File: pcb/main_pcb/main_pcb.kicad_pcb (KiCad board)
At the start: 2 copper layers, 80 x 100 mm, 58 parts, among them J1 Conn_01x05, J10 Conn_01x06_Male, J11 Conn_01x04, J12 Screw_Terminal_01x02, J13 Conn_01x02_Male, J2 Conn_01x05, J3 Conn_01x05, J4 Conn_01x05, J5 Conn_01x05, J6 Conn_01x05, J7 Conn_01x04, J8 Conn_01x06_Male, J9 Conn_01x04, Q1 Q_PMOS_GDS, SW1 SW_SPDT, U1 LSM6DSO, U2 Teensy_4.1, U3 DRV8833, U4 LM1117-3.3, U5 TPIC74101

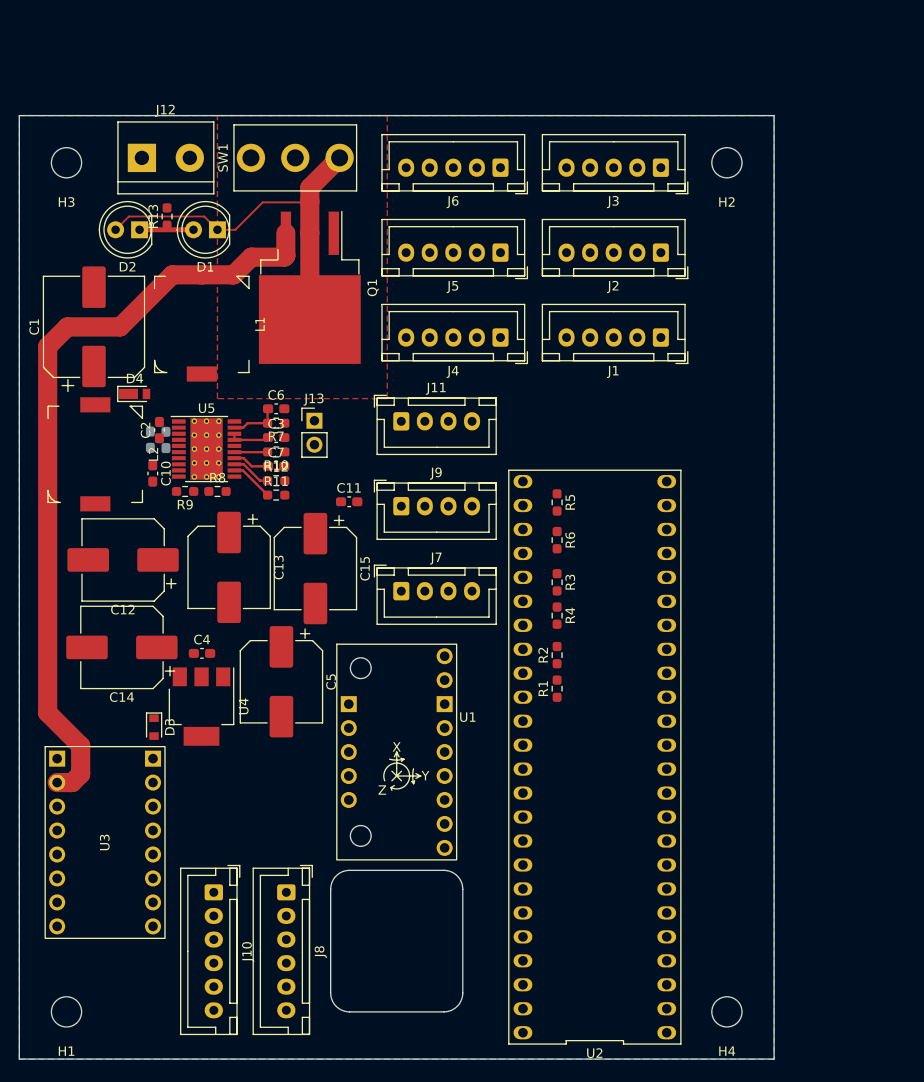
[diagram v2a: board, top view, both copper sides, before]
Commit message: Complete digital routing
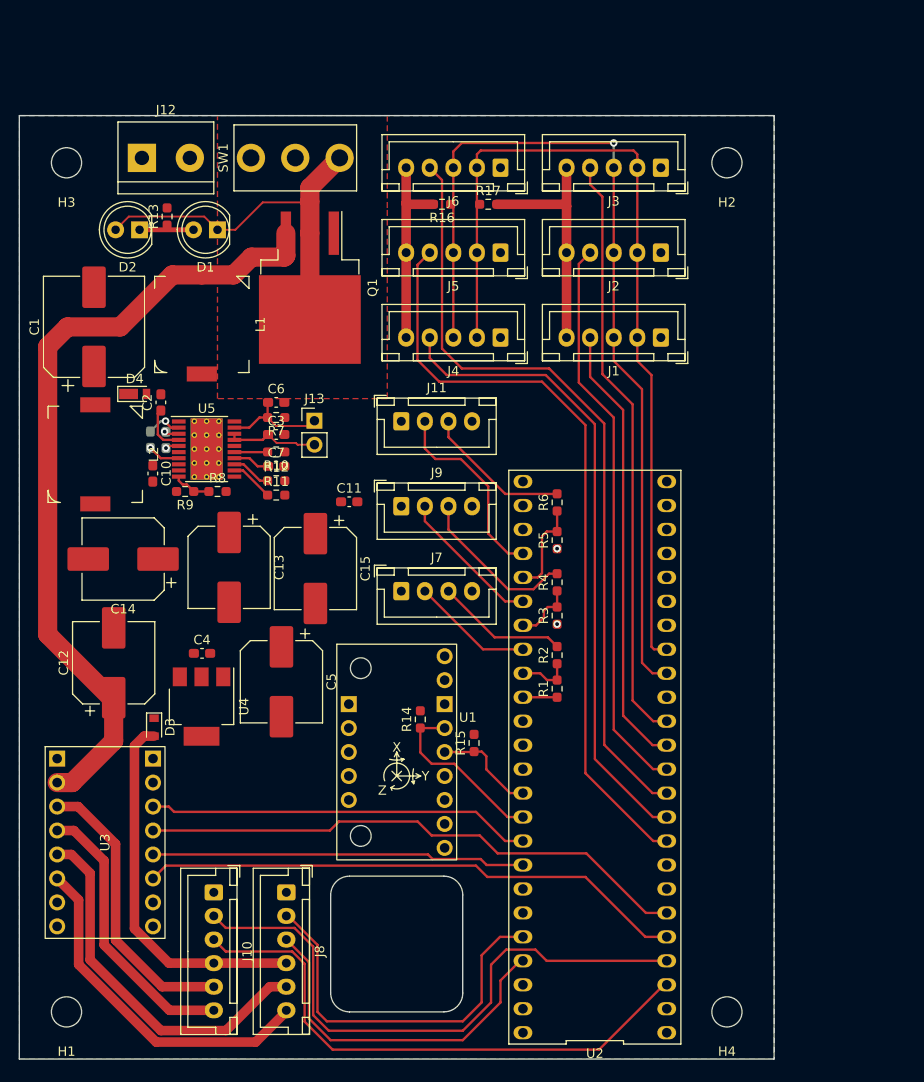
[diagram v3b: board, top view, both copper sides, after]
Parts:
- added R14: 2.2k, Resistor_SMD:R_0603_1608Metric_Pad0.98x0.95mm_HandSolder, F.Cu at (92.5, 114.0)
- added R15: 2.2k, Resistor_SMD:R_0603_1608Metric_Pad0.98x0.95mm_HandSolder, F.Cu at (98.2, 116.5)
- added R16: 2.2k, Resistor_SMD:R_0603_1608Metric_Pad0.98x0.95mm_HandSolder, F.Cu at (94.8, 59.4)
- added R17: 2.2k, Resistor_SMD:R_0603_1608Metric_Pad0.98x0.95mm_HandSolder, F.Cu at (99.7, 59.4)
- moved C12 10.9 mm to (60.0, 108.0), turned to 90 degrees
- moved C14 9.37 mm to (61.0, 97.0)
- moved R5 4.00 mm to (107.0, 95.0), turned to 90 degrees
- moved R6 4.00 mm to (107.0, 91.0), turned to 90 degrees
- moved R3 3.53 mm to (107.0, 103.0), turned to 90 degrees
- moved R4 3.53 mm to (107.0, 99.5), turned to 90 degrees
- moved C2 2.94 mm to (65.0, 80.4)
- moved C6 0.68 mm to (77.2, 80.4)
- moved R7 0.60 mm to (77.2, 82.0)
- moved C3 0.33 mm to (77.2, 83.8)
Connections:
- C12 pad 1: +5V -> +BATT
- U2 pad 10: /microcontroller/LCS5 -> /microcontroller/LCS4
- U2 pad 12: /microcontroller/LCS1 -> /microcontroller/LCS2
- U2 pad 13: /microcontroller/LCS2 -> /microcontroller/LCS1
- U2 pad 9: /microcontroller/LCS1 -> /microcontroller/LCS5
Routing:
- net /microcontroller/SCL2: track 0.00 -> 96.5 mm, vias 0 -> 1
- net /microcontroller/SDA2: track 0.00 -> 91.3 mm
- net +3V3: track 0.00 -> 85.9 mm
- net /microcontroller/LCS6: track 0.00 -> 83.0 mm
- net /microcontroller/LCS5: track 0.00 -> 81.1 mm
- net /microcontroller/LCS4: track 0.00 -> 68.2 mm
- net /microcontroller/BEQ2: track 0.00 -> 63.7 mm
- net /microcontroller/LCS3: track 0.00 -> 62.9 mm
- net /microcontroller/LCS2: track 0.00 -> 60.0 mm
- net /microcontroller/BEQ1: track 0.00 -> 59.3 mm
- net /microcontroller/BIN2: track 0.00 -> 58.9 mm
- net /microcontroller/AIN1: track 0.00 -> 58.1 mm
- net /microcontroller/LCS1: track 0.00 -> 47.4 mm
- net /microcontroller/BIN1: track 0.00 -> 40.7 mm
- net /microcontroller/AEQ2: track 0.00 -> 40.5 mm
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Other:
- outline, holes or cut-outs redrawn

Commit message: More routing
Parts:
- moved C8 1.05 mm to (63.9, 85.4)
- moved C10 0.96 mm to (64.1, 88.9)
- moved C4 0.89 mm to (70.2, 107.0)
- moved C15 0.13 mm to (81.4, 97.9)
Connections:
- U2 pad 27: GND -> unconnected-(U2-Pad27)
- U2 pad 47: (no net) -> GND
- U5 pad 21: (no net) -> GND
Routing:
- net +5V: track 0.00 -> 93.2 mm, vias 0 -> 1
- net +5VD: track 0.00 -> 92.9 mm, vias 0 -> 1
- net +3V3: track 85.9 -> 144.3 mm, vias 0 -> 1
- net GND: track 3.72 -> 14.9 mm, vias 2 -> 66
- net Net-(C8-Pad2): track 3.85 -> 4.94 mm
- added copper zone on F.Cu, net GND
- added copper zone on F.Cu, net Net-(C1-Pad1)
- added copper zone on F.Cu, net Net-(C8-Pad1)
- added copper zone on F.Cu, net Net-(C9-Pad1)
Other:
- board text added: "Rotate J1-3 to move 3v3 to outside"

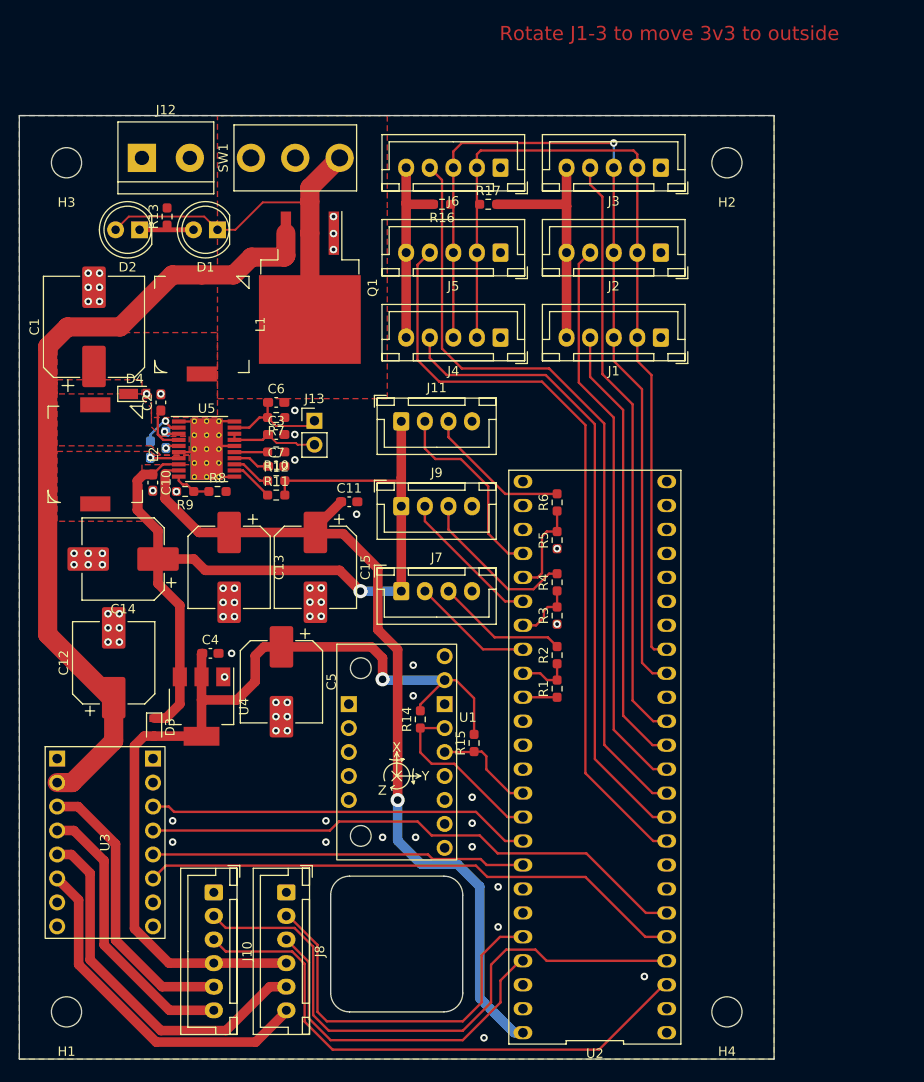
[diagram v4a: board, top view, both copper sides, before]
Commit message: Complete initial routing
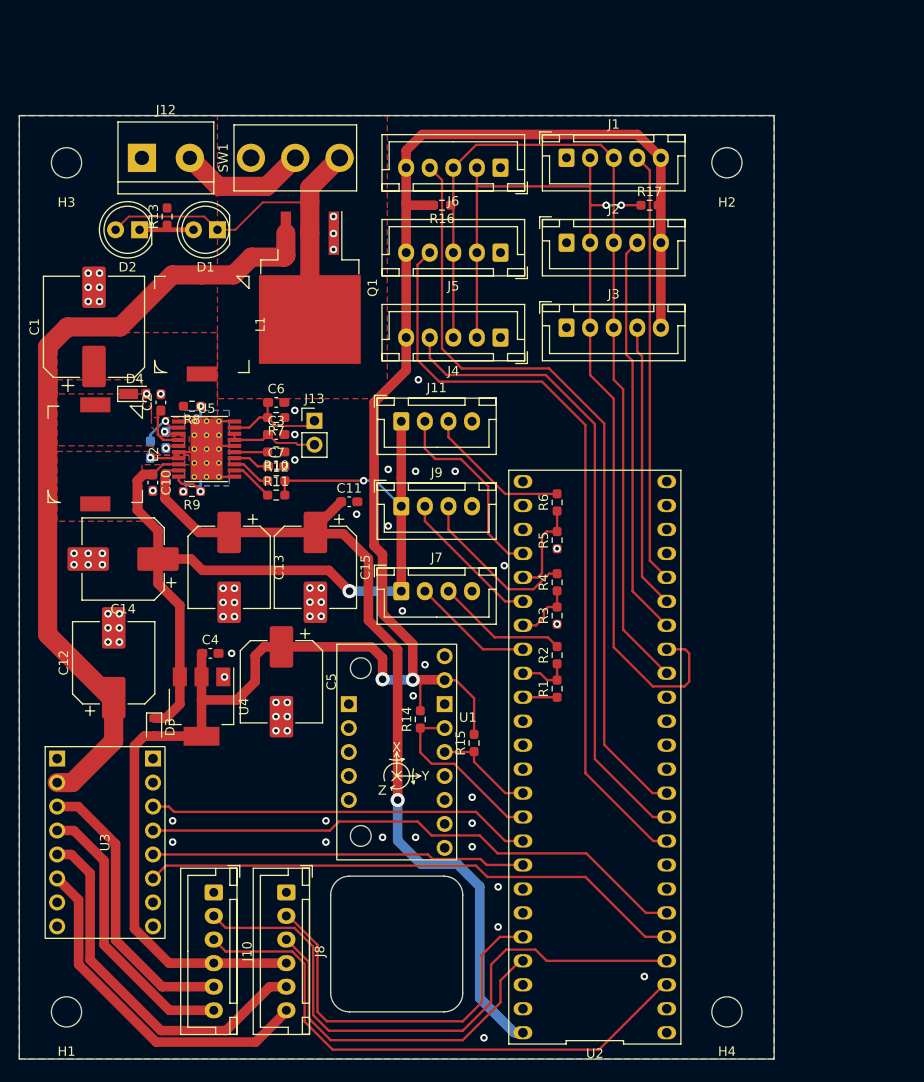
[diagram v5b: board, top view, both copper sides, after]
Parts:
- moved J1 21.5 mm to (108.0, 54.5), turned to 0 degrees
- moved J3 19.7 mm to (108.0, 72.5), turned to 0 degrees
- moved R17 17.1 mm to (116.8, 59.5)
- moved J2 10.1 mm to (108.0, 63.5), turned to 0 degrees
- moved R8 9.44 mm to (68.3, 80.8), turned to 180 degrees
- moved R9 0.72 mm to (68.3, 89.8)
- moved R16 0.10 mm to (94.8, 59.5)
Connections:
- U2 pad 12: /microcontroller/LCS2 -> unconnected-(U2-Pad12)
- U2 pad 13: /microcontroller/LCS1 -> unconnected-(U2-Pad13)
- U2 pad 14: /microcontroller/LCS3 -> unconnected-(U2-Pad14)
- U2 pad 18: unconnected-(U2-Pad18) -> /microcontroller/LCS2
- U2 pad 19: unconnected-(U2-Pad19) -> /microcontroller/LCS3
- U2 pad 20: unconnected-(U2-Pad20) -> /microcontroller/LCS1
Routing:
- net +3V3: track 144.3 -> 208.4 mm, vias 1 -> 2
- net /microcontroller/LCS3: track 62.9 -> 30.3 mm
- net /microcontroller/LCS2: track 60.0 -> 42.8 mm
- net Net-(J12-Pad2): track 0.00 -> 13.7 mm
- net /microcontroller/SDA2: track 91.3 -> 103.9 mm, vias 0 -> 2
- net Net-(R8-Pad1): track 4.10 -> 12.3 mm, vias 0 -> 2
- net /microcontroller/SCL2: track 96.5 -> 93.5 mm, vias 1 -> 0
- net /microcontroller/LCS1: track 47.4 -> 45.8 mm
- net +5V: track 93.2 -> 94.7 mm, vias 1 -> 2
- net GND: vias 66 -> 73
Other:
- board text added: "{ "ViaStitching": "0.1", "stitch_zone_0": { "HSpacing": "5", "VSpacing": "5", "Clearance": "0", "Randomize": false } }"
- board text removed: "Rotate J1-3 to move 3v3 to outside"

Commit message: Complete routing and Silkscreen
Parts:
- added D5: LED, LED_THT:LED_D5.0mm, F.Cu at (126.2, 133.5)
- added D6: LED, LED_THT:LED_D5.0mm, F.Cu at (126.3, 127.0)
- added D7: LED, LED_THT:LED_D5.0mm, F.Cu at (126.3, 120.5)
- added D8: LED, LED_THT:LED_D5.0mm, F.Cu at (126.3, 114.0)
- added G***: CWRUbotix, custom_footprints:LOGO_cwrubotix, F.Cu at (125.0, 82.7)
- added G***: LOGO, custom_footprints:pololu, F.Cu at (125.0, 69.2)
- added R18: 470, Resistor_SMD:R_0603_1608Metric_Pad0.98x0.95mm_HandSolder, F.Cu at (125.2, 138.0)
- added R19: 470, Resistor_SMD:R_0603_1608Metric_Pad0.98x0.95mm_HandSolder, F.Cu at (125.2, 139.8)
- added R20: 470, Resistor_SMD:R_0603_1608Metric_Pad0.98x0.95mm_HandSolder, F.Cu at (125.2, 107.8)
- added R21: 470, Resistor_SMD:R_0603_1608Metric_Pad0.98x0.95mm_HandSolder, F.Cu at (125.2, 109.5)
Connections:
- U2 pad 12: unconnected-(U2-Pad12) -> /microcontroller/LED2
- U2 pad 13: unconnected-(U2-Pad13) -> /microcontroller/LED3
- U2 pad 7: unconnected-(U2-Pad7) -> /microcontroller/LED0
- U2 pad 8: unconnected-(U2-Pad8) -> /microcontroller/LED1
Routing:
- net Net-(D6-Pad1): track 0.00 -> 15.0 mm
- net Net-(D7-Pad1): track 0.00 -> 14.9 mm
- net /microcontroller/LED3: track 0.00 -> 6.25 mm
- net /microcontroller/LED1: track 0.00 -> 6.12 mm
- net /microcontroller/LED0: track 0.00 -> 5.72 mm
- net /microcontroller/LED2: track 0.00 -> 5.62 mm
- net Net-(D5-Pad1): track 0.00 -> 4.64 mm
- net Net-(D8-Pad1): track 0.00 -> 4.55 mm
- net +BATT: track 84.1 -> 82.5 mm
- net GND: vias 73 -> 161
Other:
- board text added: "(-)"
- board text added: "CRRCT"
- board text added: "Corinthian Ewesuedo"
- board text added: "HW Team: Zach Baldwin Nehal Garg"
- board text added: "LDAR1"
- board text added: "LDAR2"
- board text added: "LDAR3"
- board text added: "LDAR4"
- board text added: "LDAR5"
- board text added: "LDAR6"
- board text added: "LED0"
- board text added: "LED1"
- board text added: "LED2"
- board text added: "LED3"
- board text added: "MOTOR A"
- board text added: "MOTOR B"
- board text added: "Micromouse 2022-2023"
- board text added: "Micromouse Controller HW Design REV: 1.0 Layout REV: A Order No."
- board text added: "ON"
- board text added: "RVRSE"
- board text added: "T4 PWR"
- board text added: "Teensy 4.1"
- board text added: "USNC1"
- board text added: "USNC2"
- board text added: "USNC3"
- board text removed: "TODO: * Add Micromouse * Add designers' names * Add Pololu logo * HWrev info"

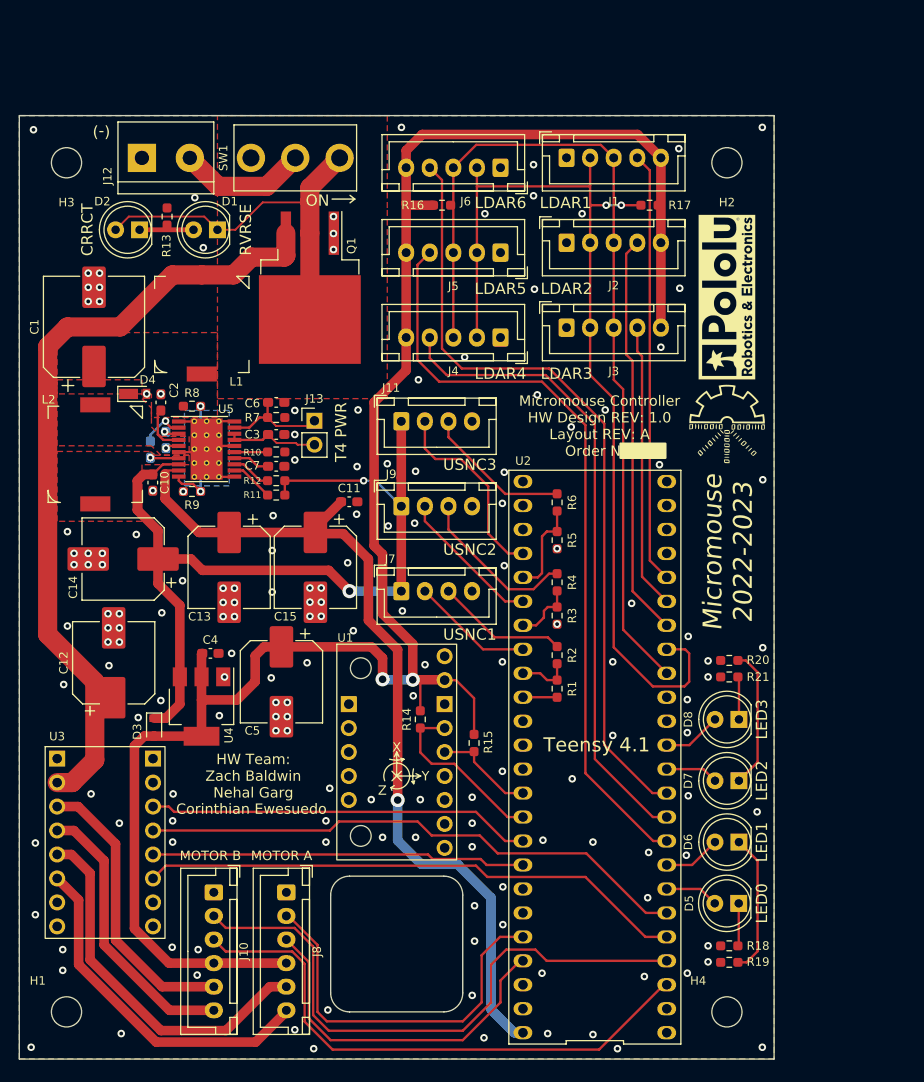
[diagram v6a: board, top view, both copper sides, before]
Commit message: Fix many DRC errors; correct motor B sig names
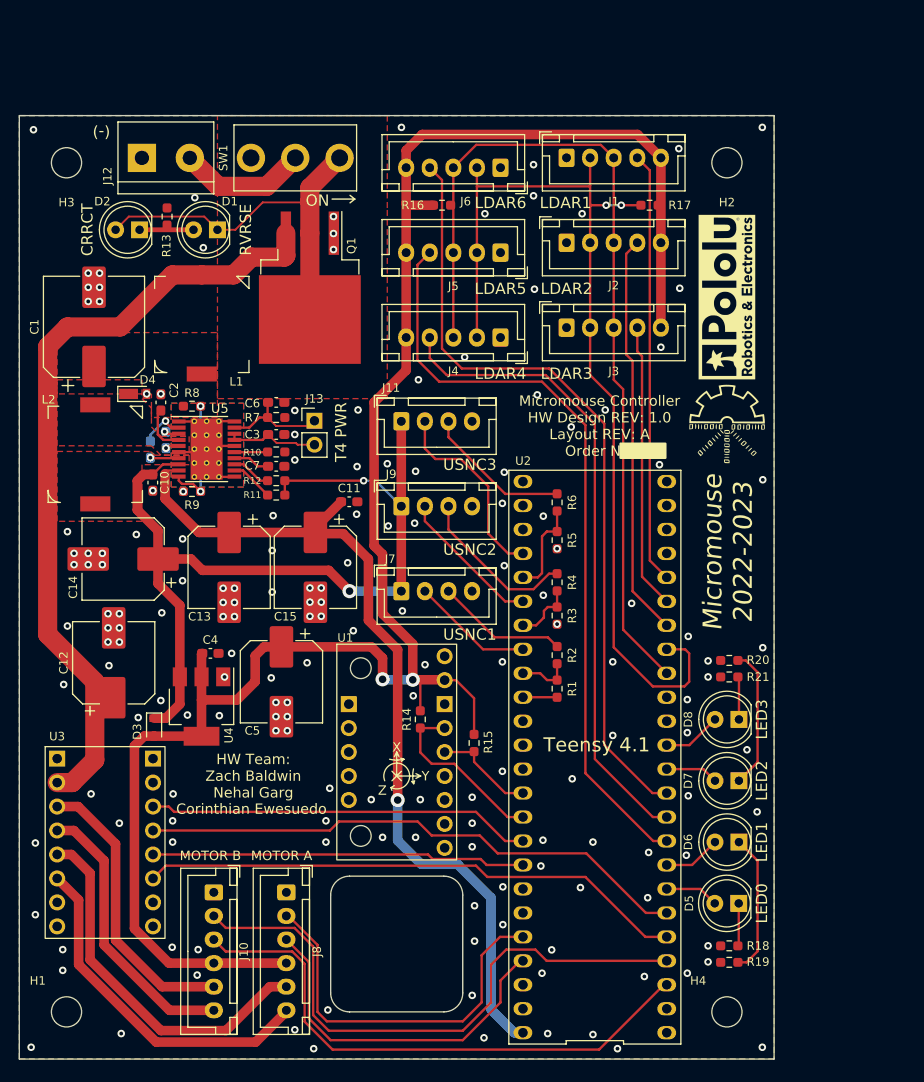
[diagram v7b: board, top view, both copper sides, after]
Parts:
- G***: footprint custom_footprints:pololu -> custom_footprints:LOGO_pololu
- U5: footprint Package_SO:HTSSOP-20-1EP_4.4x6.5mm_P0.65mm_EP3.4x6.5mm_ThermalVias -> custom_footprints:HTSSOP-20-1EP_4.4x6.5mm_P0.65mm_EP3.4x6.5mm_ThermalVias
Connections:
- J10 pad 5: /microcontroller/BOUT2 -> /microcontroller/BOUT1
- J10 pad 6: /microcontroller/BOUT1 -> /microcontroller/BOUT2
- U3 pad 3: /microcontroller/BOUT2 -> /microcontroller/BOUT1
- U3 pad 4: /microcontroller/BOUT1 -> /microcontroller/BOUT2
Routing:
- net GND: track 14.9 -> 13.7 mm, vias 161 -> 169
- net Net-(C6-Pad1): track 11.1 -> 10.3 mm
- net +5VD: track 92.9 -> 92.1 mm
- net /microcontroller/BOUT2: track 30.5 -> 29.7 mm
- net /microcontroller/BOUT1: track 29.7 -> 30.5 mm
